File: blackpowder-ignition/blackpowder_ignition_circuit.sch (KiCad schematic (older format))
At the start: 6 parts, among them J2 Conn_01x02, Q1 FDS6898A

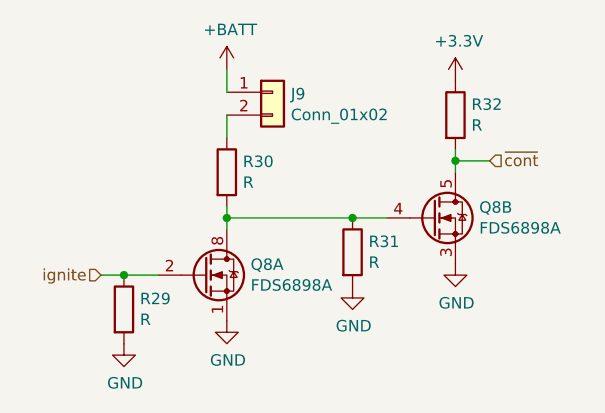
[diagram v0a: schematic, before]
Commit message: added hierarchical sch sheet for bus, address jummper pads, connections from io expander to subcircuits
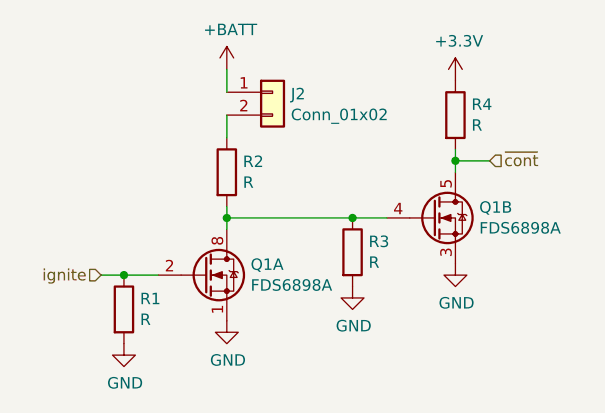
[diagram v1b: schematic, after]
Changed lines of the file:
@@
 $Descr A4 11693 8268
 encoding utf-8
-Sheet 9 9
+Sheet 2 8
 Title ""
 Date ""
@@
 AR Path="/5EB223EE/5EAFF725" Ref="Q7"  Part="1"
 AR Path="/5EB223F2/5EAFF725" Ref="Q8"  Part="1"
-F 0 "Q8" H 4404 4046 50  0000 L CNN
+F 0 "Q1" H 4404 4046 50  0000 L CNN
 F 1 "FDS6898A" H 4404 3955 50  0000 L CNN
 F 2 "Package_SO:SOIC-8_3.9x4.9mm_P1.27mm" H 4400 3925 50  0001 L CIN
@@
 AR Path="/5EB223EE/5EAFF72B" Ref="R25"  Part="1"
 AR Path="/5EB223F2/5EAFF72B" Ref="R29"  Part="1"
-F 0 "R29" H 3920 4196 50  0000 L CNN
+F 0 "R1" H 3920 4196 50  0000 L CNN
 F 1 "R" H 3920 4105 50  0000 L CNN
 F 2 "Resistor_SMD:R_0603_1608Metric_Pad1.05x0.95mm_HandSolder" V 3780 4150 50  0001 C CNN
@@
 AR Path="/5EB223EE/5EAFF731" Ref="R26"  Part="1"
 AR Path="/5EB223F2/5EAFF731" Ref="R30"  Part="1"
-F 0 "R30" H 4370 3596 50  0000 L CNN
+F 0 "R2" H 4370 3596 50  0000 L CNN
 F 1 "R" H 4370 3505 50  0000 L CNN
 F 2 "star-common-lib:PWR163" V 4230 3550 50  0001 C CNN
@@
 AR Path="/5EB223EE/5EAFF737" Ref="R27"  Part="1"
 AR Path="/5EB223F2/5EAFF737" Ref="R31"  Part="1"
-F 0 "R31" H 4920 3946 50  0000 L CNN
+F 0 "R3" H 4920 3946 50  0000 L CNN
 F 1 "R" H 4920 3855 50  0000 L CNN
 F 2 "Resistor_SMD:R_0603_1608Metric_Pad1.05x0.95mm_HandSolder" V 4780 3900 50  0001 C CNN
@@
 AR Path="/5EB223EE/5EAFF73D" Ref="Q7"  Part="2"
 AR Path="/5EB223F2/5EAFF73D" Ref="Q8"  Part="2"
-F 0 "Q8" H 5404 3796 50  0000 L CNN
+F 0 "Q1" H 5404 3796 50  0000 L CNN
 F 1 "FDS6898A" H 5404 3705 50  0000 L CNN
 F 2 "Package_SO:SOIC-8_3.9x4.9mm_P1.27mm" H 5400 3675 50  0001 L CIN
@@
 AR Path="/5EB223EE/5EAFF743" Ref="R28"  Part="1"
 AR Path="/5EB223F2/5EAFF743" Ref="R32"  Part="1"
-F 0 "R32" H 5370 3346 50  0000 L CNN
+F 0 "R4" H 5370 3346 50  0000 L CNN
 F 1 "R" H 5370 3255 50  0000 L CNN
 F 2 "Resistor_SMD:R_0603_1608Metric_Pad1.05x0.95mm_HandSolder" V 5230 3300 50  0001 C CNN
@@
 AR Path="/5EB223EE/5EAFF758" Ref="#PWR0137"  Part="1"
 AR Path="/5EB223F2/5EAFF758" Ref="#PWR0143"  Part="1"
-F 0 "#PWR0143" H 3850 4050 50  0001 C CNN
+F 0 "#PWR0101" H 3850 4050 50  0001 C CNN
 F 1 "GND" H 3855 4127 50  0000 C CNN
 F 2 "" H 3850 4300 50  0001 C CNN
@@
 AR Path="/5EB223EE/5EAFF75E" Ref="#PWR0138"  Part="1"
 AR Path="/5EB223F2/5EAFF75E" Ref="#PWR0144"  Part="1"
-F 0 "#PWR0144" H 4300 3950 50  0001 C CNN
+F 0 "#PWR0102" H 4300 3950 50  0001 C CNN
 F 1 "GND" H 4305 4027 50  0000 C CNN
 F 2 "" H 4300 4200 50  0001 C CNN
@@
 AR Path="/5EB223EE/5EAFF764" Ref="#PWR0139"  Part="1"
 AR Path="/5EB223F2/5EAFF764" Ref="#PWR0145"  Part="1"
-F 0 "#PWR0145" H 5300 3700 50  0001 C CNN
+F 0 "#PWR0103" H 5300 3700 50  0001 C CNN
 F 1 "GND" H 5305 3777 50  0000 C CNN
 F 2 "" H 5300 3950 50  0001 C CNN
@@
 AR Path="/5EB223EE/5EAFF76A" Ref="#PWR0140"  Part="1"
 AR Path="/5EB223F2/5EAFF76A" Ref="#PWR0146"  Part="1"
-F 0 "#PWR0146" H 4850 3800 50  0001 C CNN
+F 0 "#PWR0104" H 4850 3800 50  0001 C CNN
 F 1 "GND" H 4855 3877 50  0000 C CNN
 F 2 "" H 4850 4050 50  0001 C CNN
@@
 AR Path="/5EB223EE/5EAFF770" Ref="#PWR0141"  Part="1"
 AR Path="/5EB223F2/5EAFF770" Ref="#PWR0147"  Part="1"
-F 0 "#PWR0147" H 5300 3000 50  0001 C CNN
+F 0 "#PWR0105" H 5300 3000 50  0001 C CNN
 F 1 "+3.3V" H 5315 3323 50  0000 C CNN
 F 2 "" H 5300 3150 50  0001 C CNN
@@
 AR Path="/5EB223EE/5EAFF776" Ref="#PWR0142"  Part="1"
 AR Path="/5EB223F2/5EAFF776" Ref="#PWR0148"  Part="1"
-F 0 "#PWR0148" H 4300 2950 50  0001 C CNN
+F 0 "#PWR0106" H 4300 2950 50  0001 C CNN
 F 1 "+BATT" H 4315 3273 50  0000 C CNN
 F 2 "" H 4300 3100 50  0001 C CNN
@@
 AR Path="/5EB223EE/5EAFF77D" Ref="J8"  Part="1"
 AR Path="/5EB223F2/5EAFF77D" Ref="J9"  Part="1"
-F 0 "J9" H 4580 3192 50  0000 L CNN
+F 0 "J2" H 4580 3192 50  0000 L CNN
 F 1 "Conn_01x02" H 4580 3101 50  0000 L CNN
 F 2 "Connector_Molex:Molex_Mini-Fit_Jr_5569-02A2_2x01_P4.20mm_Horizontal" H 4500 3200 50  0001 C CNN

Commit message: added power connector
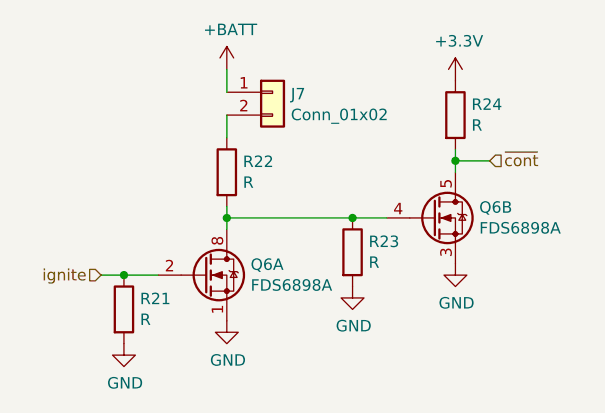
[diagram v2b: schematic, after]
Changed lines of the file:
@@
 AR Path="/5EB223EE/5EAFF725" Ref="Q7"  Part="1"
 AR Path="/5EB223F2/5EAFF725" Ref="Q8"  Part="1"
-F 0 "Q1" H 4404 4046 50  0000 L CNN
+F 0 "Q6" H 4404 4046 50  0000 L CNN
 F 1 "FDS6898A" H 4404 3955 50  0000 L CNN
 F 2 "Package_SO:SOIC-8_3.9x4.9mm_P1.27mm" H 4400 3925 50  0001 L CIN
@@
 AR Path="/5EB223EE/5EAFF72B" Ref="R25"  Part="1"
 AR Path="/5EB223F2/5EAFF72B" Ref="R29"  Part="1"
-F 0 "R1" H 3920 4196 50  0000 L CNN
+F 0 "R21" H 3920 4196 50  0000 L CNN
 F 1 "R" H 3920 4105 50  0000 L CNN
 F 2 "Resistor_SMD:R_0603_1608Metric_Pad1.05x0.95mm_HandSolder" V 3780 4150 50  0001 C CNN
@@
 AR Path="/5EB223EE/5EAFF731" Ref="R26"  Part="1"
 AR Path="/5EB223F2/5EAFF731" Ref="R30"  Part="1"
-F 0 "R2" H 4370 3596 50  0000 L CNN
+F 0 "R22" H 4370 3596 50  0000 L CNN
 F 1 "R" H 4370 3505 50  0000 L CNN
 F 2 "star-common-lib:PWR163" V 4230 3550 50  0001 C CNN
@@
 AR Path="/5EB223EE/5EAFF737" Ref="R27"  Part="1"
 AR Path="/5EB223F2/5EAFF737" Ref="R31"  Part="1"
-F 0 "R3" H 4920 3946 50  0000 L CNN
+F 0 "R23" H 4920 3946 50  0000 L CNN
 F 1 "R" H 4920 3855 50  0000 L CNN
 F 2 "Resistor_SMD:R_0603_1608Metric_Pad1.05x0.95mm_HandSolder" V 4780 3900 50  0001 C CNN
@@
 AR Path="/5EB223EE/5EAFF73D" Ref="Q7"  Part="2"
 AR Path="/5EB223F2/5EAFF73D" Ref="Q8"  Part="2"
-F 0 "Q1" H 5404 3796 50  0000 L CNN
+F 0 "Q6" H 5404 3796 50  0000 L CNN
 F 1 "FDS6898A" H 5404 3705 50  0000 L CNN
 F 2 "Package_SO:SOIC-8_3.9x4.9mm_P1.27mm" H 5400 3675 50  0001 L CIN
@@
 AR Path="/5EB223EE/5EAFF743" Ref="R28"  Part="1"
 AR Path="/5EB223F2/5EAFF743" Ref="R32"  Part="1"
-F 0 "R4" H 5370 3346 50  0000 L CNN
+F 0 "R24" H 5370 3346 50  0000 L CNN
 F 1 "R" H 5370 3255 50  0000 L CNN
 F 2 "Resistor_SMD:R_0603_1608Metric_Pad1.05x0.95mm_HandSolder" V 5230 3300 50  0001 C CNN
@@
 AR Path="/5EB223EE/5EAFF758" Ref="#PWR0137"  Part="1"
 AR Path="/5EB223F2/5EAFF758" Ref="#PWR0143"  Part="1"
-F 0 "#PWR0101" H 3850 4050 50  0001 C CNN
+F 0 "#PWR0131" H 3850 4050 50  0001 C CNN
 F 1 "GND" H 3855 4127 50  0000 C CNN
 F 2 "" H 3850 4300 50  0001 C CNN
@@
 AR Path="/5EB223EE/5EAFF75E" Ref="#PWR0138"  Part="1"
 AR Path="/5EB223F2/5EAFF75E" Ref="#PWR0144"  Part="1"
-F 0 "#PWR0102" H 4300 3950 50  0001 C CNN
+F 0 "#PWR0132" H 4300 3950 50  0001 C CNN
 F 1 "GND" H 4305 4027 50  0000 C CNN
 F 2 "" H 4300 4200 50  0001 C CNN
@@
 AR Path="/5EB223EE/5EAFF764" Ref="#PWR0139"  Part="1"
 AR Path="/5EB223F2/5EAFF764" Ref="#PWR0145"  Part="1"
-F 0 "#PWR0103" H 5300 3700 50  0001 C CNN
+F 0 "#PWR0133" H 5300 3700 50  0001 C CNN
 F 1 "GND" H 5305 3777 50  0000 C CNN
 F 2 "" H 5300 3950 50  0001 C CNN
@@
 AR Path="/5EB223EE/5EAFF76A" Ref="#PWR0140"  Part="1"
 AR Path="/5EB223F2/5EAFF76A" Ref="#PWR0146"  Part="1"
-F 0 "#PWR0104" H 4850 3800 50  0001 C CNN
+F 0 "#PWR0134" H 4850 3800 50  0001 C CNN
 F 1 "GND" H 4855 3877 50  0000 C CNN
 F 2 "" H 4850 4050 50  0001 C CNN
@@
 AR Path="/5EB223EE/5EAFF770" Ref="#PWR0141"  Part="1"
 AR Path="/5EB223F2/5EAFF770" Ref="#PWR0147"  Part="1"
-F 0 "#PWR0105" H 5300 3000 50  0001 C CNN
+F 0 "#PWR0135" H 5300 3000 50  0001 C CNN
 F 1 "+3.3V" H 5315 3323 50  0000 C CNN
 F 2 "" H 5300 3150 50  0001 C CNN
@@
 AR Path="/5EB223EE/5EAFF776" Ref="#PWR0142"  Part="1"
 AR Path="/5EB223F2/5EAFF776" Ref="#PWR0148"  Part="1"
-F 0 "#PWR0106" H 4300 2950 50  0001 C CNN
+F 0 "#PWR0136" H 4300 2950 50  0001 C CNN
 F 1 "+BATT" H 4315 3273 50  0000 C CNN
 F 2 "" H 4300 3100 50  0001 C CNN
@@
 AR Path="/5EB223EE/5EAFF77D" Ref="J8"  Part="1"
 AR Path="/5EB223F2/5EAFF77D" Ref="J9"  Part="1"
-F 0 "J2" H 4580 3192 50  0000 L CNN
+F 0 "J7" H 4580 3192 50  0000 L CNN
 F 1 "Conn_01x02" H 4580 3101 50  0000 L CNN
 F 2 "Connector_Molex:Molex_Mini-Fit_Jr_5569-02A2_2x01_P4.20mm_Horizontal" H 4500 3200 50  0001 C CNN

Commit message: initial layout
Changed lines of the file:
@@
 $Descr A4 11693 8268
 encoding utf-8
-Sheet 2 8
+Sheet 3 8
 Title ""
 Date ""
@@
 AR Path="/5EB223EE/5EAFF725" Ref="Q7"  Part="1"
 AR Path="/5EB223F2/5EAFF725" Ref="Q8"  Part="1"
-F 0 "Q6" H 4404 4046 50  0000 L CNN
+F 0 "Q2" H 4404 4046 50  0000 L CNN
 F 1 "FDS6898A" H 4404 3955 50  0000 L CNN
 F 2 "Package_SO:SOIC-8_3.9x4.9mm_P1.27mm" H 4400 3925 50  0001 L CIN
@@
 AR Path="/5EB223EE/5EAFF72B" Ref="R25"  Part="1"
 AR Path="/5EB223F2/5EAFF72B" Ref="R29"  Part="1"
-F 0 "R21" H 3920 4196 50  0000 L CNN
+F 0 "R5" H 3920 4196 50  0000 L CNN
 F 1 "R" H 3920 4105 50  0000 L CNN
 F 2 "Resistor_SMD:R_0603_1608Metric_Pad1.05x0.95mm_HandSolder" V 3780 4150 50  0001 C CNN
@@
 AR Path="/5EB223EE/5EAFF731" Ref="R26"  Part="1"
 AR Path="/5EB223F2/5EAFF731" Ref="R30"  Part="1"
-F 0 "R22" H 4370 3596 50  0000 L CNN
+F 0 "R6" H 4370 3596 50  0000 L CNN
 F 1 "R" H 4370 3505 50  0000 L CNN
 F 2 "star-common-lib:PWR163" V 4230 3550 50  0001 C CNN
@@
 AR Path="/5EB223EE/5EAFF737" Ref="R27"  Part="1"
 AR Path="/5EB223F2/5EAFF737" Ref="R31"  Part="1"
-F 0 "R23" H 4920 3946 50  0000 L CNN
+F 0 "R7" H 4920 3946 50  0000 L CNN
 F 1 "R" H 4920 3855 50  0000 L CNN
 F 2 "Resistor_SMD:R_0603_1608Metric_Pad1.05x0.95mm_HandSolder" V 4780 3900 50  0001 C CNN
@@
 AR Path="/5EB223EE/5EAFF73D" Ref="Q7"  Part="2"
 AR Path="/5EB223F2/5EAFF73D" Ref="Q8"  Part="2"
-F 0 "Q6" H 5404 3796 50  0000 L CNN
+F 0 "Q2" H 5404 3796 50  0000 L CNN
 F 1 "FDS6898A" H 5404 3705 50  0000 L CNN
 F 2 "Package_SO:SOIC-8_3.9x4.9mm_P1.27mm" H 5400 3675 50  0001 L CIN
@@
 AR Path="/5EB223EE/5EAFF743" Ref="R28"  Part="1"
 AR Path="/5EB223F2/5EAFF743" Ref="R32"  Part="1"
-F 0 "R24" H 5370 3346 50  0000 L CNN
+F 0 "R8" H 5370 3346 50  0000 L CNN
 F 1 "R" H 5370 3255 50  0000 L CNN
 F 2 "Resistor_SMD:R_0603_1608Metric_Pad1.05x0.95mm_HandSolder" V 5230 3300 50  0001 C CNN
@@
 AR Path="/5EB223EE/5EAFF77D" Ref="J8"  Part="1"
 AR Path="/5EB223F2/5EAFF77D" Ref="J9"  Part="1"
-F 0 "J7" H 4580 3192 50  0000 L CNN
+F 0 "J3" H 4580 3192 50  0000 L CNN
 F 1 "Conn_01x02" H 4580 3101 50  0000 L CNN
 F 2 "Connector_Molex:Molex_Mini-Fit_Jr_5569-02A2_2x01_P4.20mm_Horizontal" H 4500 3200 50  0001 C CNN
